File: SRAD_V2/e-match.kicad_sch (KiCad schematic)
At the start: 27 parts, among them IC5 NCV81071BZR2G, IC6 NCV81071BZR2G, J10 691210910002, J11 691210910002, J7 DC Jack, J8 691210910002, J9 691210910002, M2 FDC8878, Q10 FDD1600N10ALZ, Q6 AOSP36326C, Q7 AOSP36326C, Q8 AOSP36326C, Q9 AOSP36326C, U21 TMCS1108A2UQDR

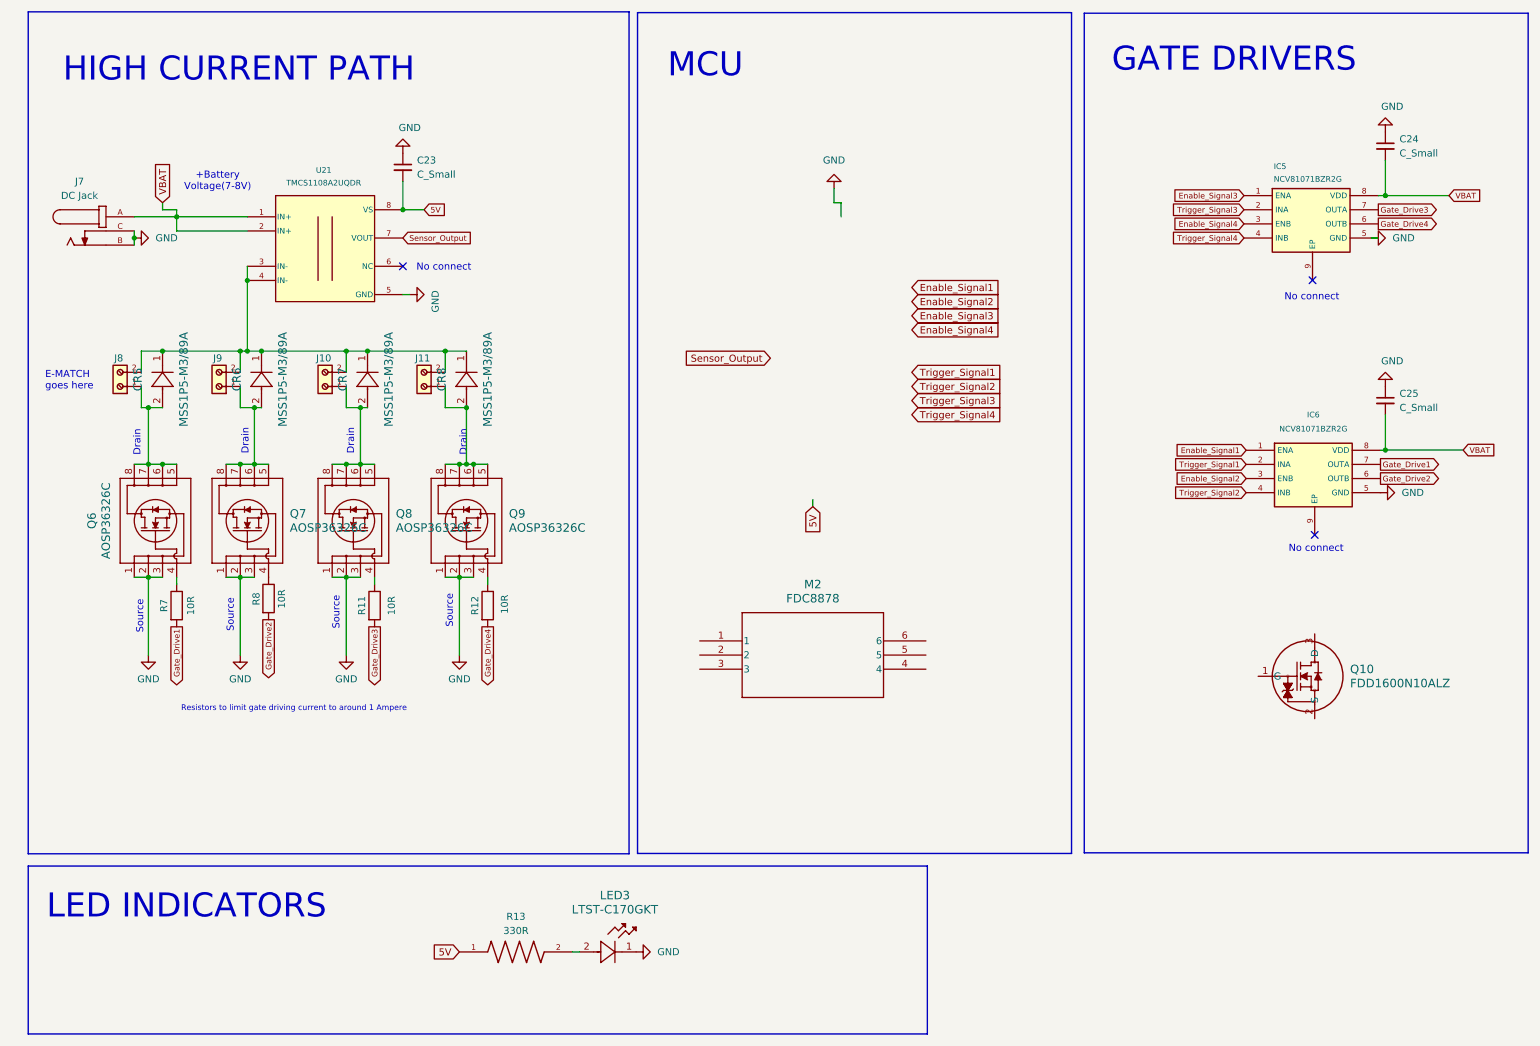
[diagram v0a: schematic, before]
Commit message: created some basic building blocks as hierarchical sheets
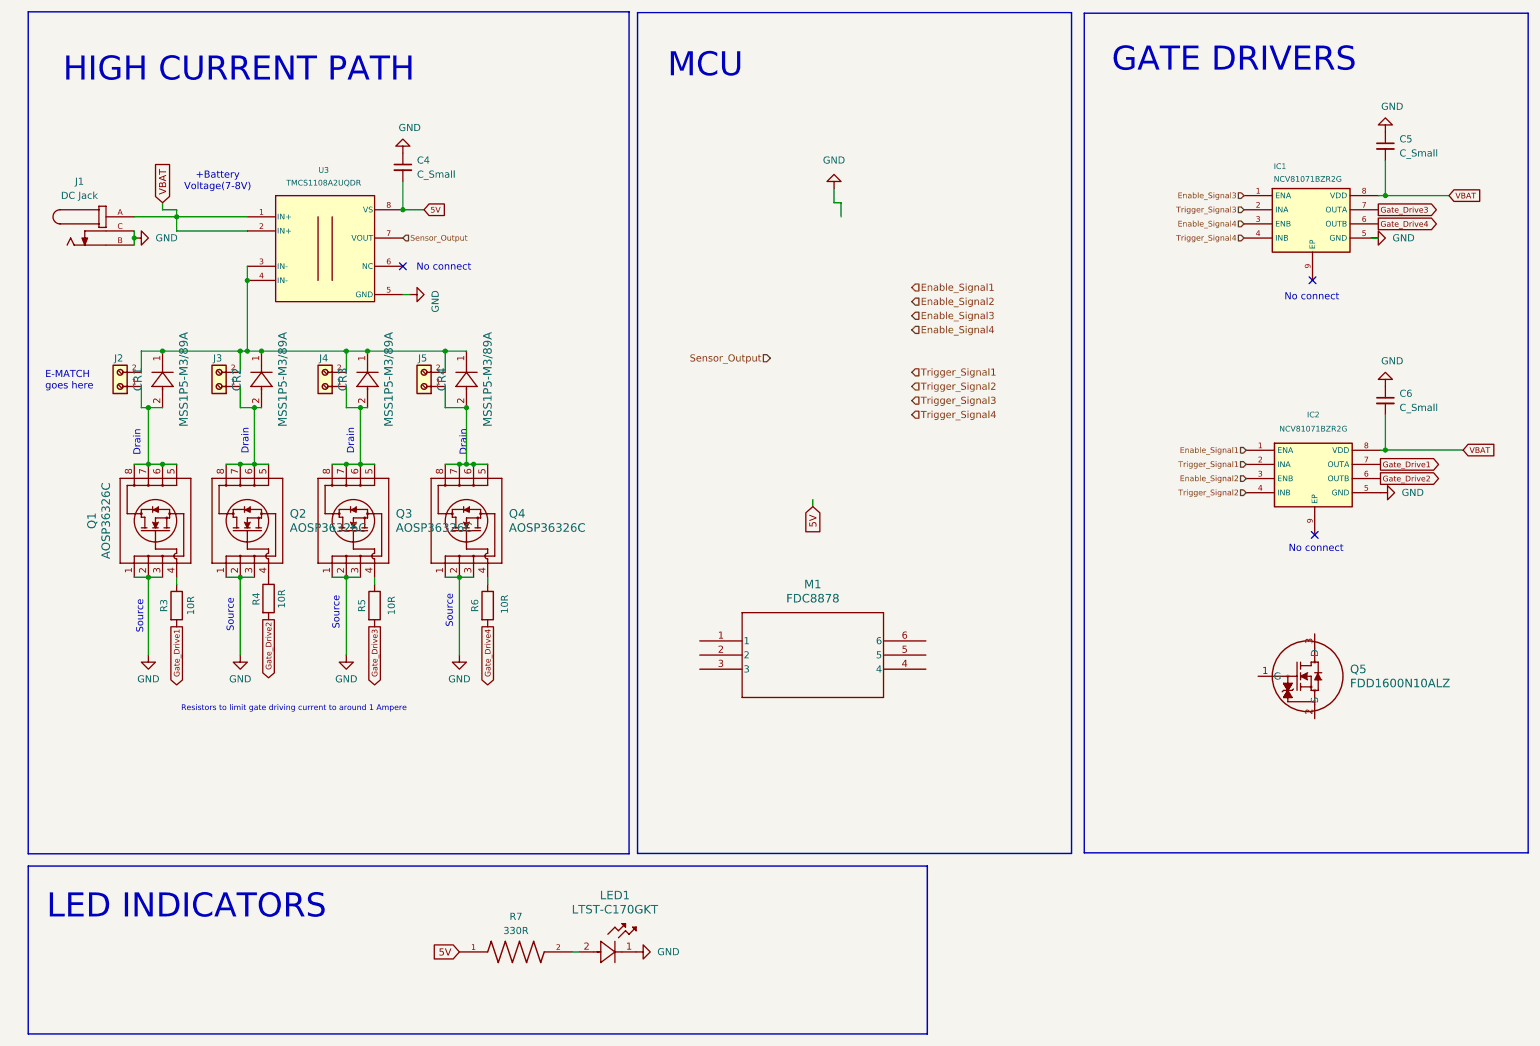
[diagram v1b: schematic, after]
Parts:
- renumbered C23 to C4, C24 to C5, C25 to C6, CR5 to CR1, CR6 to CR2, CR7 to CR3, CR8 to CR4, IC5 to IC1, IC6 to IC2, J7 to J1, J8 to J2, J9 to J3, J10 to J4, J11 to J5, LED3 to LED1, M2 to M1, Q6 to Q1, Q7 to Q2, Q8 to Q3, Q9 to Q4, Q10 to Q5, R7 to R3, R8 to R4, R11 to R5, R12 to R6, R13 to R7, U21 to U3

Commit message: linked 3-d models
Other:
- note removed: "MCU"
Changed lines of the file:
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@@
-	)
-	(rectangle
-		(start 123.444 11.5719)
-		(end 201.422 162.643)
-		(stroke
-			(width 0.254)
-			(type default)
-		)
-		(fill
-			(type none)
-		)
 	)
 	(rectangle
@@
 		)
 	)
-	(text "MCU"
-		(exclude_from_sim no)
-		(at 135.636 21.082 0)
-		(effects
-			(font
-				(size 4.318 4.318)
-			)
-		)
-	)
 	(text "Drain"
 		(exclude_from_sim no)
@@
 	(wire
 		(pts
-			(xy 158.75 45.72) (xy 158.75 43.18)
-		)
-		(stroke
-			(width 0)
-			(type default)
-		)
-	)
-	(wire
-		(pts
 			(xy 52.07 92.71) (xy 54.61 92.71)
 		)
@@
 	(wire
 		(pts
-			(xy 160.02 48.26) (xy 160.02 45.72)
-		)
-		(stroke
-			(width 0)
-			(type default)
-		)
-	)
-	(wire
-		(pts
 			(xy 257.81 83.82) (xy 257.81 90.17)
 		)
@@
 		(pts
 			(xy 52.07 82.55) (xy 54.61 82.55)
-		)
-		(stroke
-			(width 0)
-			(type default)
-		)
-	)
-	(wire
-		(pts
-			(xy 154.94 100.33) (xy 154.94 99.06)
-		)
-		(stroke
-			(width 0)
-			(type default)
-		)
-	)
-	(wire
-		(pts
-			(xy 160.02 45.72) (xy 158.75 45.72)
 		)
 		(stroke
@@
 	(global_label "5V"
 		(shape input)
-		(at 154.94 100.33 270)
-		(fields_autoplaced yes)
-		(effects
-			(font
-				(size 1.27 1.27)
-			)
-			(justify right)
-		)
-		(property "Intersheetrefs" "${INTERSHEET_REFS}"
-			(at 154.94 105.6133 90)
-			(effects
-				(font
-					(size 1.27 1.27)
-				)
-				(justify right)
-				(hide yes)
-			)
-		)
-	)
-	(global_label "5V"
-		(shape input)
 		(at 91.44 180.34 180)
 		(fields_autoplaced yes)
@@
 		)
 	)
-	(hierarchical_label "Enable_Signal3"
-		(shape input)
-		(at 172.72 66.04 0)
-		(effects
-			(font
-				(size 1.27 1.27)
-			)
-			(justify left)
-		)
-	)
-	(hierarchical_label "Trigger_Signal3"
-		(shape input)
-		(at 172.72 81.28 0)
-		(effects
-			(font
-				(size 1.27 1.27)
-			)
-			(justify left)
-		)
-	)
 	(hierarchical_label "Trigger_Signal1"
 		(shape input)
@@
 		)
 	)
-	(hierarchical_label "Enable_Signal2"
-		(shape input)
-		(at 172.72 63.5 0)
-		(effects
-			(font
-				(size 1.27 1.27)
-			)
-			(justify left)
-		)
-	)
 	(hierarchical_label "Trigger_Signal2"
 		(shape input)
@@
 		)
 	)
-	(hierarchical_label "Trigger_Signal4"
-		(shape input)
-		(at 172.72 83.82 0)
-		(effects
-			(font
-				(size 1.27 1.27)
-			)
-			(justify left)
-		)
-	)
-	(hierarchical_label "Sensor_Output"
-		(shape input)
-		(at 147.32 73.66 180)
-		(effects
-			(font
-				(size 1.27 1.27)
-			)
-			(justify right)
-		)
-	)
-	(hierarchical_label "Enable_Signal4"
-		(shape input)
-		(at 172.72 68.58 0)
-		(effects
-			(font
-				(size 1.27 1.27)
-			)
-			(justify left)
-		)
-	)
 	(hierarchical_label "Sensor_Output"
 		(shape input)
@@
 	(hierarchical_label "Enable_Signal1"
 		(shape input)
-		(at 172.72 60.96 0)
-		(effects
-			(font
-				(size 1.27 1.27)
-			)
-			(justify left)
-		)
-	)
-	(hierarchical_label "Trigger_Signal1"
-		(shape input)
-		(at 172.72 76.2 0)
-		(effects
-			(font
-				(size 1.27 1.27)
-			)
-			(justify left)
-		)
-	)
-	(hierarchical_label "Enable_Signal1"
-		(shape input)
 		(at 232.7997 90.2051 180)
 		(effects
@@
 			)
 			(justify right)
-		)
-	)
-	(hierarchical_label "Trigger_Signal2"
-		(shape input)
-		(at 172.72 78.74 0)
-		(effects
-			(font
-				(size 1.27 1.27)
-			)
-			(justify left)
 		)
 	)
@@
 					(unit 1)
 				)
-			)
-		)
-	)
-	(symbol
-		(lib_id "power:GND")
-		(at 158.75 43.18 180)
-		(unit 1)
-		(exclude_from_sim no)
-		(in_bom yes)
-		(on_board yes)
-		(dnp no)
-		(fields_autoplaced yes)
-		(property "Reference" "#PWR010"
-			(at 158.75 36.83 0)
-			(effects
-				(font
-					(size 1.27 1.27)
-				)
-				(hide yes)
-			)
-		)
-		(property "Value" "GND"
-			(at 158.75 38.1 0)
-			(effects
-				(font
-					(size 1.27 1.27)
-				)
-			)
-		)
-		(property "Footprint" ""
-			(at 158.75 43.18 0)
-			(effects
-				(font
-					(size 1.27 1.27)
-				)
-				(hide yes)
-			)
-		)
-		(property "Datasheet" ""
-			(at 158.75 43.18 0)
-			(effects
-				(font
-					(size 1.27 1.27)
-				)
-				(hide yes)
-			)
-		)
-		(property "Description" "Power symbol creates a global label with name \"GND\" , ground"
-			(at 158.75 43.18 0)
-			(effects
-				(font
-					(size 1.27 1.27)
-				)
-				(hide yes)
-			)
-		)
-		(pin "1"
-		)
-		(instances
-			(project "SRAD_V2"
-				(path "/016ea6e5-09c6-43d4-b6cc-3404e2d65458/a2059f4c-c92f-483b-9b86-061767cb943d"
-					(reference "#PWR010")
-					(unit 1)
-				)

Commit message: more changes
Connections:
- net Enable_Signal1: no longer names the net of IC2.1 (ENA)
- net Enable_Signal2: no longer names the net of IC2.3 (ENB)
- net Enable_Signal3: no longer names the net of IC1.1 (ENA)
- net Enable_Signal4: no longer names the net of IC1.3 (ENB)
- net Sensor_Output renamed IVAL
- net Trigger_Signal1 renamed CH1
- net Trigger_Signal2 renamed CH2
- net Trigger_Signal3 renamed CH3
- net Trigger_Signal4 renamed CH4

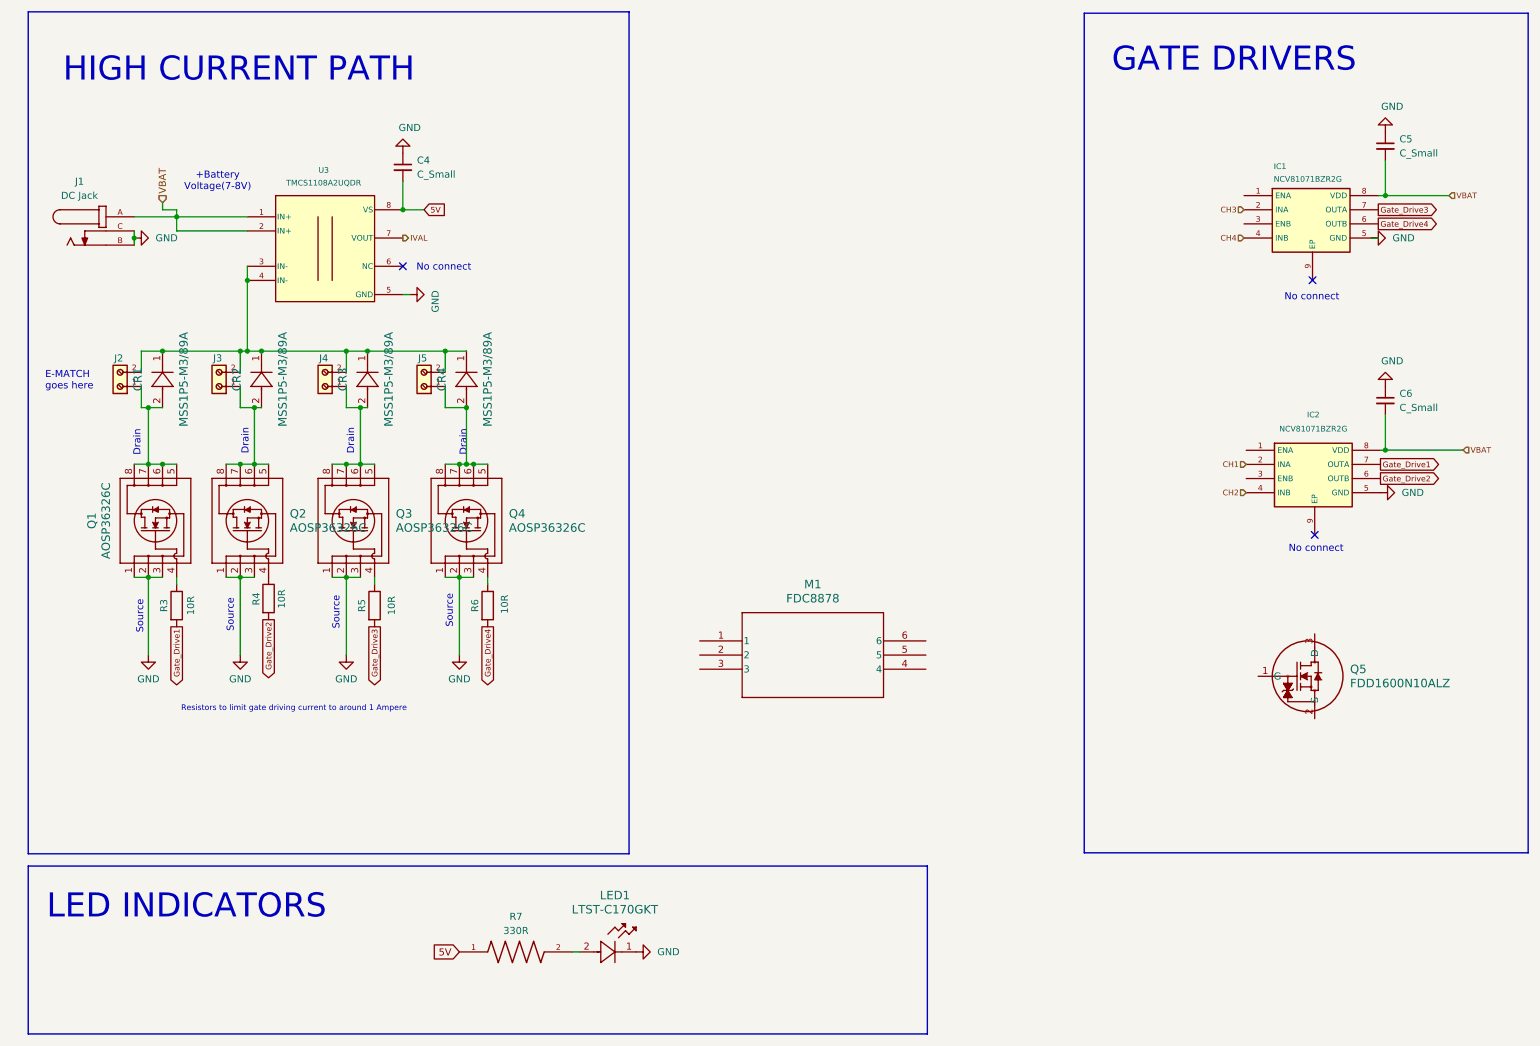
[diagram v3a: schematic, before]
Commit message: new connector
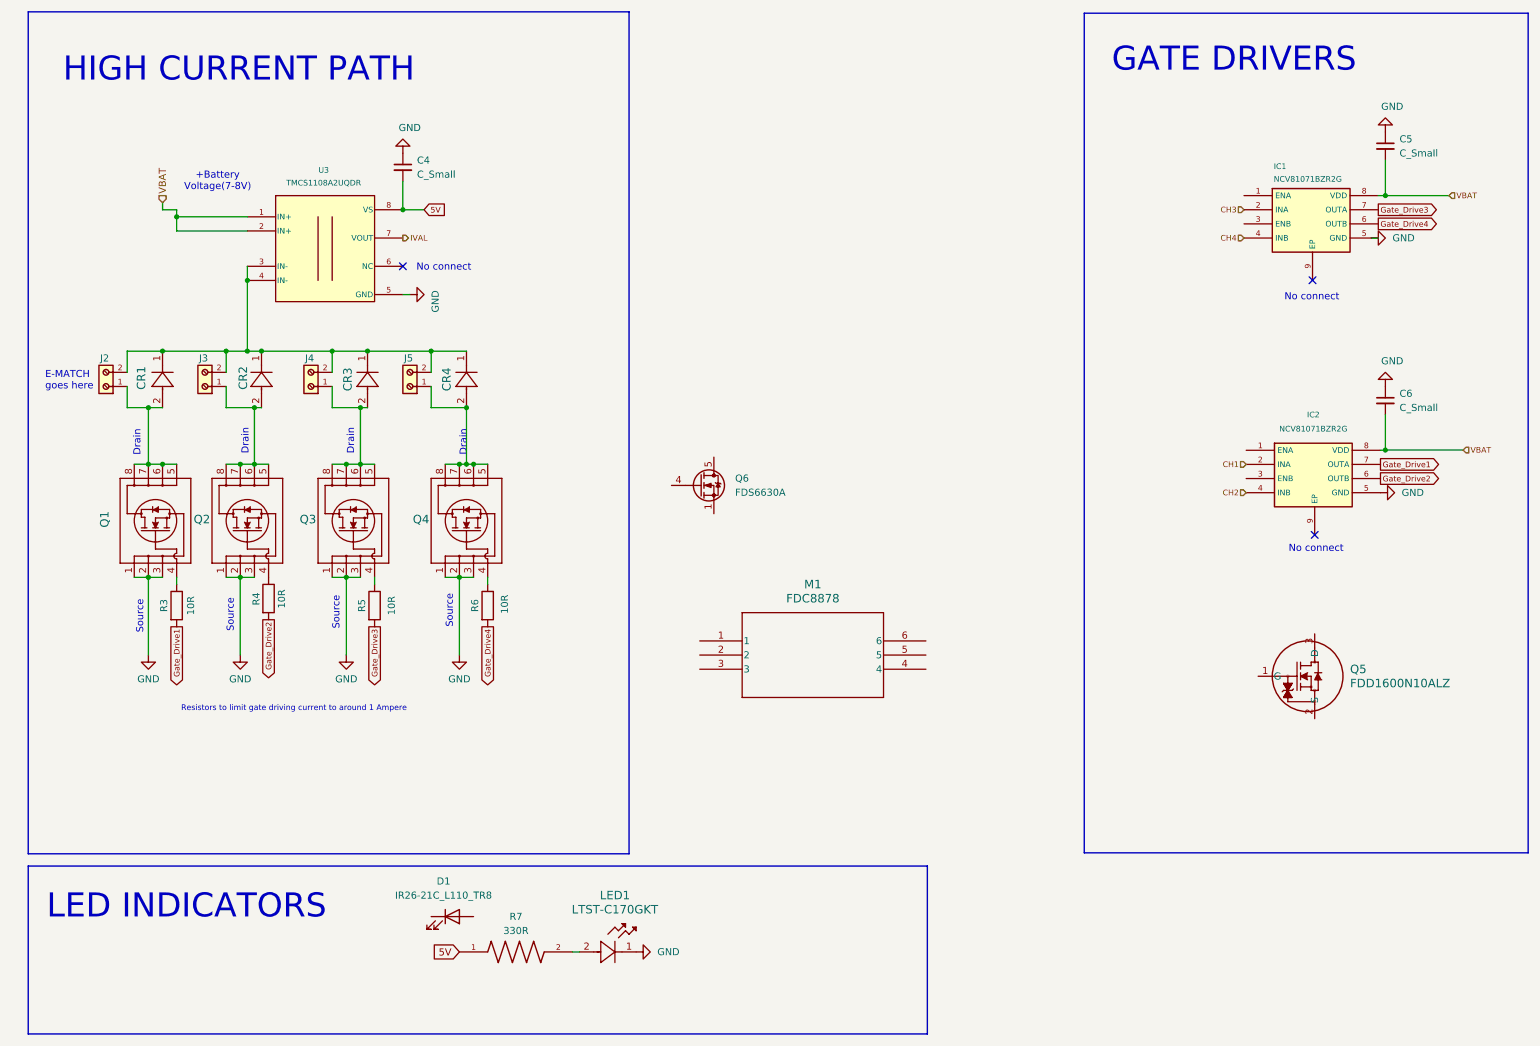
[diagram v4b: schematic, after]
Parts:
- removed J1: DC Jack, DC-Jack:TENSILITY_54-00130, symbol DC Jack:54-00130
- added D1: IR26-21C_L110_TR8, LED_SMD:LED_1206_3216Metric, symbol LED:IR26-21C_L110_TR8
- added Q6: FDS6630A, Package_SO:SOIC-8_3.9x4.9mm_P1.27mm, symbol Transistor_FET:FDS6630A
- R3, R4, R5, R6: footprint Gate Resistor:RES_RC1206_YAG -> Resistor_SMD:R_0603_1608Metric
- R7: footprint SMD_RESISTOR:RESC1608X55N -> Resistor_SMD:R_0603_1608Metric
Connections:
- new net: Q6.1 (S), Q6.2 (S), Q6.3 (S)
- new net: Q6.5 (D), Q6.6 (D), Q6.7 (D), Q6.8 (D)
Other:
- moved on the sheet: J2, J3, J4, J5

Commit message: tinkered with the layout
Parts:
- removed Q5: FDD1600N10ALZ, FDD1600N10ALZ:TO252_FDD1600_ONS-L, symbol FDD1600N10ALZ:FDD1600N10ALZ
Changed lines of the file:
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@@
-	)
-	(symbol
-		(lib_id "FDD1600N10ALZ:FDD1600N10ALZ")
-		(at 234.95 130.81 0)
-		(unit 1)
-		(exclude_from_sim no)
-		(in_bom yes)
-		(on_board yes)
-		(dnp no)
-		(fields_autoplaced yes)
-		(property "Reference" "Q5"
-			(at 251.46 129.5399 0)
-			(effects
-				(font
-					(size 1.524 1.524)
-				)
-				(justify left)
-			)
-		)
-		(property "Value" "FDD1600N10ALZ"
-			(at 251.46 132.0799 0)
-			(effects
-				(font
-					(size 1.524 1.524)
-				)
-				(justify left)
-			)
-		)
-		(property "Footprint" "FDD1600N10ALZ:TO252_FDD1600_ONS-L"
-			(at 234.95 130.81 0)
-			(effects
-				(font
-					(size 1.27 1.27)
-					(italic yes)
-				)
-				(hide yes)
-			)
-		)
-		(property "Datasheet" "FDD1600N10ALZ"
-			(at 234.95 130.81 0)
-			(effects
-				(font
-					(size 1.27 1.27)
-					(italic yes)
-				)
-				(hide yes)
-			)
-		)
-		(property "Description" ""
-			(at 234.95 130.81 0)
-			(effects
-				(font
-					(size 1.27 1.27)
-				)
-				(hide yes)
-			)
-		)
-		(pin "1"
-		)
-		(pin "3"
-		)
-		(pin "2"
-		)
-		(instances
-			(project "SRAD_V2"
-				(path "/016ea6e5-09c6-43d4-b6cc-3404e2d65458/a2059f4c-c92f-483b-9b86-061767cb943d"
-					(reference "Q5")
-					(unit 1)
-				)
-			)
-		)
 	)
 	(symbol
